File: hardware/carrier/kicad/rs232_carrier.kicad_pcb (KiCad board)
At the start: 2 copper layers, 78 x 95 mm, 133 parts, among them J1 WS header 1-14, J11 RJ45, J12 RJ45, J13 RJ45, J14 RJ45, J2 WS header 15-28, J3 EXT, Q11 2N7002, Q12 AO3401A, Q21 2N7002, Q22 AO3401A, Q31 2N7002, Q32 AO3401A, Q41 2N7002, Q42 AO3401A, U101 TLP2361, U102 TLP2361, U103 MAX3232E, U104 74LVC1G17, U201 TLP2361, U202 TLP2361, U203 MAX3232E, U204 74LVC1G17, U301 TLP2361, U302 TLP2361, U303 MAX3232E, U304 74LVC1G17, U401 TLP2361, U402 TLP2361, U403 MAX3232E, U404 74LVC1G17, U5 MT3608

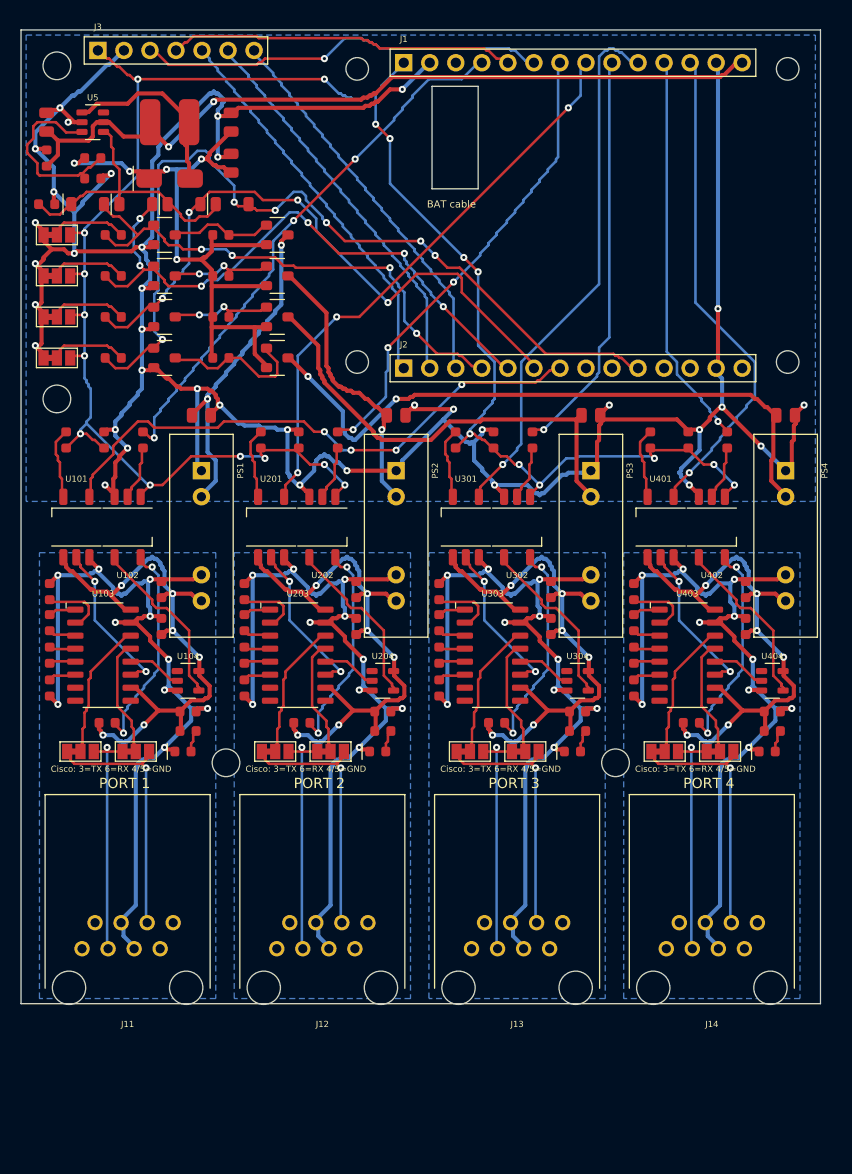
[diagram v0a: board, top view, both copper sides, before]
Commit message: Hardware 0.2: Modul hochkant, Gehäuse zum Zusammenstecken, Akkuklappe
Trägerplatine 78 × 107 mm: Waveshare-Modul hochkant mit USB-C an der
Stirnseite, Versorgung daneben, JST-PH für den Akku auf der Unterseite.
Gehäuse aus drei Teilen ohne Schrauben: Lippe/Nut, vier lösbare Rasthaken,
Pfosten klemmen die Platine, Displayglas als Oberseite, Akkuklappe mit
Rastlasche. Neu geroutet, KiCad-DRC ohne elektrische Fehler.

Co-Authored-By: Claude Fable 5.1 <noreply@anthropic.com>
Claude-Session: https://claude.ai/code/session_01NzB9JfE6QfygfS2yw734Lm
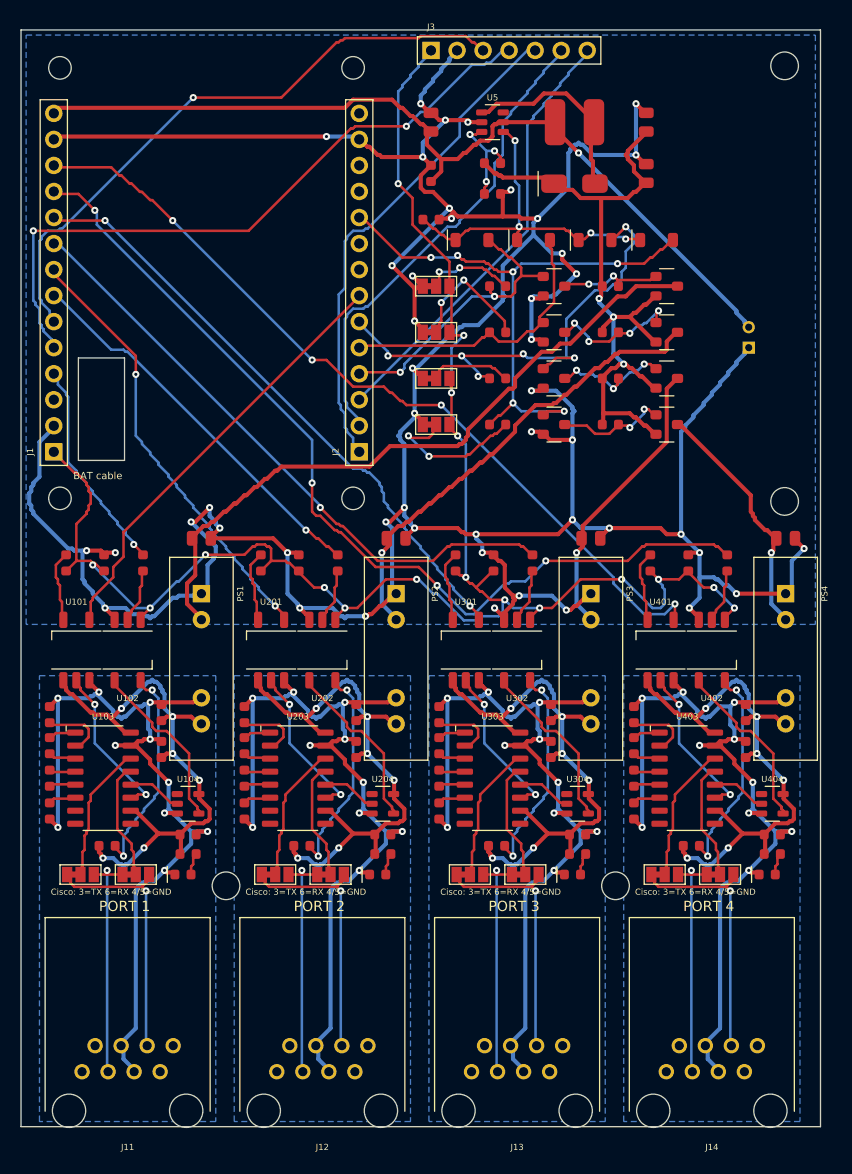
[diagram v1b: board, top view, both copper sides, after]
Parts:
- added J4: BAT JST-PH, rs232fp:JST_PH_2_Vertical, B.Cu at (71.0, 31.0)
- moved H6 71.7 mm to (74.5, 46.0)
- moved H4 71.0 mm to (3.80, 3.70)
- moved H5 71.0 mm to (74.5, 3.50)
- moved H3 51.2 mm to (32.4, 3.70)
- moved J1 51.1 mm to (3.20, 41.2), turned to 90 degrees
- moved H2 51.0 mm to (3.80, 45.7)
- moved D54 41.5 mm to (62.0, 20.5)
- moved C53 40.5 mm to (61.0, 14.0)
- moved C52 40.5 mm to (61.0, 9.00)
- moved D53 40.3 mm to (56.0, 20.5)
- moved D5 39.5 mm to (54.0, 15.0)
- moved L1 39.5 mm to (54.0, 9.00)
- moved R52 39.0 mm to (46.0, 16.0)
- moved R51 39.0 mm to (46.0, 13.0)
- moved U5 39.0 mm to (46.0, 9.00)
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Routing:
- net GND: track 312.0 -> 387.7 mm, vias 36 -> 47
- net ESP_RX4: track 38.5 -> 90.7 mm, vias 1 -> 4
- net ISO_IN4: track 63.8 -> 24.5 mm, vias 2 -> 1
- net ISO_IN1: track 31.9 -> 68.2 mm, vias 2 -> 0
- net ESP_TX4: track 48.3 -> 81.0 mm, vias 1 -> 4
- net ESP_RX1: track 53.3 -> 21.2 mm, vias 3 -> 1
- net SCL: track 34.0 -> 65.9 mm, vias 0 -> 2
- net EN2: track 59.1 -> 29.3 mm, vias 6 -> 0
- net EN4: track 85.2 -> 57.6 mm
- net EN1: track 50.8 -> 29.0 mm, vias 4 -> 2
- net ESP_RX3: track 39.7 -> 60.7 mm
- net SDA: track 40.0 -> 60.7 mm
- net ISO_IN2: track 27.9 -> 47.2 mm
- net +3V3: track 194.9 -> 178.7 mm, vias 22 -> 17
- net ISO_IN3: track 44.5 -> 29.0 mm, vias 0 -> 1
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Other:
- board size 78 x 95 mm -> 78 x 107 mm
- board text added: "Waveshare ESP32-S3-Touch-LCD-2, USB-C up"
- board text removed: "Waveshare ESP32-S3-Touch-LCD-2 (component side down), USB-C ->"

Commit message: Hardware 0.3: Modul mittig, Gehäuse aus Körper und innenliegendem Boden
Trägerplatine: Waveshare-Modul mittig, Versorgung links/rechts aufgeteilt,
RJ45 ganz in der Wand, neu geroutet, DRC ohne elektrische Fehler.
Gehäuse nach Rams/Ive: ein Körper mit durchlaufenden Radien, Glas als
Oberseite, Ziffern vertieft, Boden innenliegend mit sechs Rasthaken,
Akku und J4 nach Abnehmen des Bodens zugänglich; SMA an der Seitenwand.

Co-Authored-By: Claude Fable 5.1 <noreply@anthropic.com>
Claude-Session: https://claude.ai/code/session_01NzB9JfE6QfygfS2yw734Lm
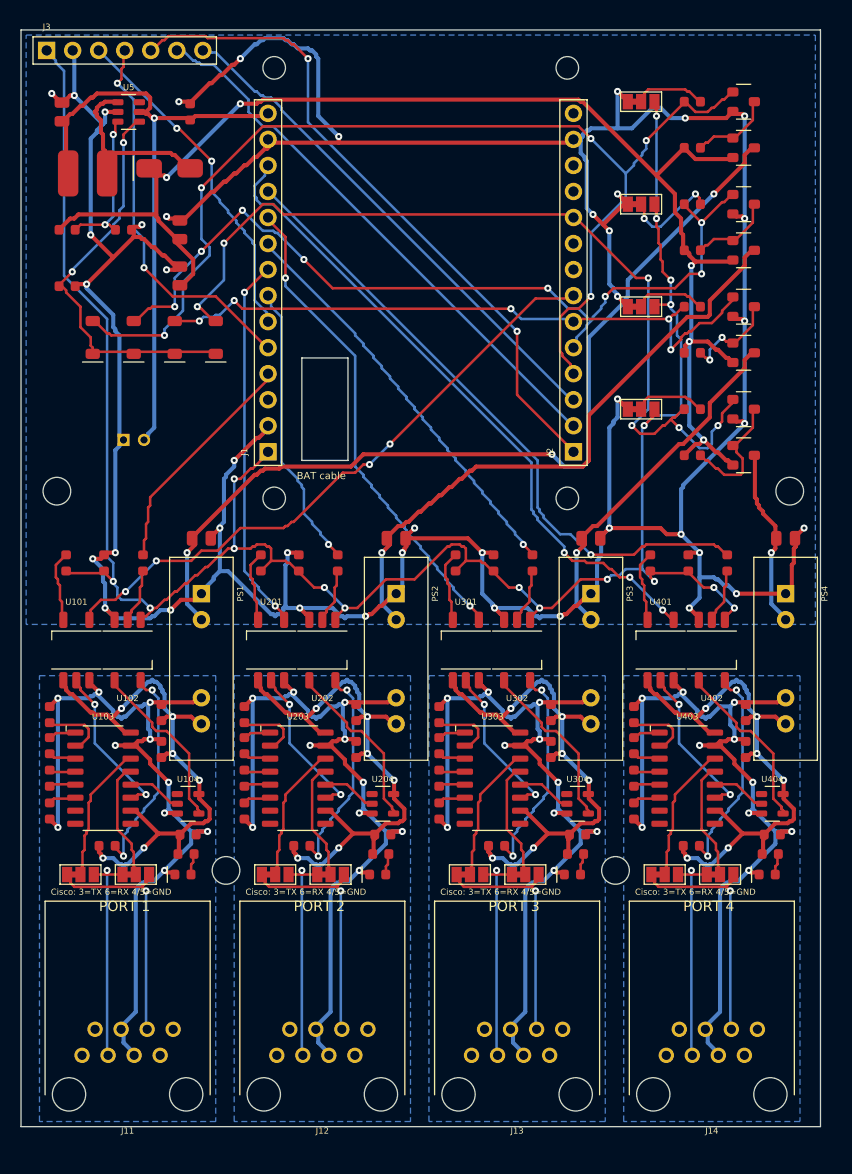
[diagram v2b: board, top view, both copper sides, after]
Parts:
- moved H5 82.2 mm to (3.50, 45.0)
- moved J4 61.7 mm to (10.0, 40.0), turned to 0 degrees
- moved L1 47.8 mm to (6.50, 14.0)
- moved C52 46.7 mm to (15.5, 19.5)
- moved C53 46.6 mm to (15.5, 24.0)
- moved D54 44.0 mm to (19.0, 30.0), turned to 90 degrees
- moved D53 42.1 mm to (15.0, 30.0), turned to 90 degrees
- moved R51 42.0 mm to (4.50, 19.5)
- moved D52 40.1 mm to (11.0, 30.0), turned to 90 degrees
- moved D5 39.5 mm to (14.5, 13.5)
- moved D51 38.2 mm to (7.00, 30.0), turned to 90 degrees
- moved J3 37.5 mm to (2.50, 2.00)
- moved R52 36.2 mm to (10.0, 19.5)
- moved R53 36.1 mm to (4.50, 25.0)
- moved C51 36.0 mm to (4.00, 8.00)
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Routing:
- net EN1: track 29.0 -> 108.7 mm, vias 2 -> 5
- net +5V: track 70.8 -> 135.6 mm, vias 3 -> 5
- net EN2: track 29.3 -> 83.3 mm, vias 0 -> 8
- net +3V3: track 178.7 -> 215.9 mm
- net EN4: track 57.6 -> 87.5 mm
- net SCL: track 65.9 -> 37.8 mm
- net ESP_RX4: track 90.7 -> 63.2 mm, vias 4 -> 1
- net SDA: track 60.7 -> 33.4 mm, vias 1 -> 2
- net VBAT: track 87.9 -> 62.7 mm
- net ISO_IN1: track 68.2 -> 89.9 mm, vias 0 -> 3
- net ESP_RX3: track 60.7 -> 41.0 mm
- net ESP_TX1: track 42.5 -> 60.7 mm, vias 0 -> 4
- net IO2: track 49.1 -> 65.9 mm, vias 0 -> 2
- net ESP_TX4: track 81.0 -> 64.9 mm, vias 4 -> 3
- net EN3: track 49.0 -> 63.6 mm, vias 6 -> 5
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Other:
- outline, holes or cut-outs redrawn

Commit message: Hardware 0.3.1: Maße aus der Waveshare-Zeichnung übernommen
Platine 35,00 × 48,20 mm, Bohrungen 29,00 × 42,20 mm, Glas 37,10 × 58,80 mm
R2,60, Stapel 7,20/9,70 mm, Stiftleisten 30,48 mm. Schaltspalte 1,5 mm nach
rechts, C10 und 2N7002 gedreht (Massepads an der Fläche), Router: Masse-
bäume ohne destruktives Auftrennen (Rip-up mit Rückrollen), Fensterecken
mit Glasradius, Vorschau- und PNG-Rendering in den Skripten, README-Prüfliste
auf die Zeichnung umgestellt.

Co-Authored-By: Claude Fable 5.1 <noreply@anthropic.com>
Claude-Session: https://claude.ai/code/session_01NzB9JfE6QfygfS2yw734Lm
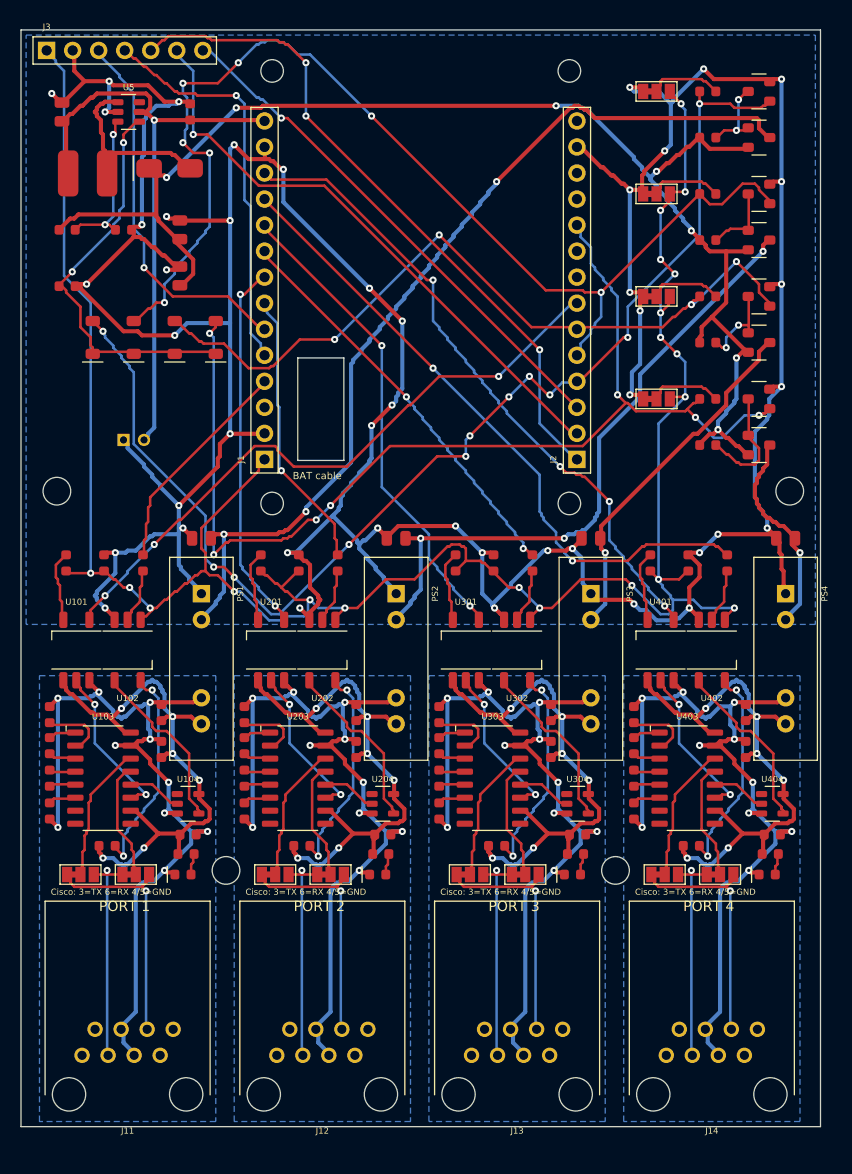
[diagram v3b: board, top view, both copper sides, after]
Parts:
- moved JP11 1.80 mm to (62.0, 6.00)
- moved JP12 1.80 mm to (62.0, 16.0)
- moved JP13 1.80 mm to (62.0, 26.0)
- moved JP14 1.80 mm to (62.0, 36.0)
- moved Q11 1.80 mm to (72.0, 6.00), turned to 180 degrees
- moved Q12 1.80 mm to (72.0, 10.5)
- moved Q21 1.80 mm to (72.0, 16.0), turned to 180 degrees
- moved Q22 1.80 mm to (72.0, 20.5)
- moved Q31 1.80 mm to (72.0, 26.0), turned to 180 degrees
- moved Q32 1.80 mm to (72.0, 30.5)
- moved Q41 1.80 mm to (72.0, 36.0), turned to 180 degrees
- moved Q42 1.80 mm to (72.0, 40.5)
- moved R61 1.80 mm to (67.0, 6.00)
- moved R62 1.80 mm to (67.0, 16.0)
- moved R63 1.80 mm to (67.0, 26.0)
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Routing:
- net EN2: track 83.3 -> 112.3 mm, vias 8 -> 7
- net EN4: track 87.5 -> 107.4 mm, vias 6 -> 7
- net GND: track 399.1 -> 415.8 mm, vias 42 -> 45
- net +3V3: track 215.9 -> 229.9 mm, vias 17 -> 20
- net EN3: track 63.6 -> 75.5 mm, vias 5 -> 4
- net EN1: track 108.7 -> 118.9 mm, vias 5 -> 11
- net SDA: track 33.4 -> 37.2 mm, vias 2 -> 1
- net IO4: track 54.6 -> 58.3 mm, vias 0 -> 1
- net ISO_IN4: track 18.4 -> 21.6 mm
- net ENP2: track 9.34 -> 7.10 mm, vias 2 -> 0
- net ESP_TX1: track 60.7 -> 62.7 mm, vias 4 -> 3
- net PG3: track 10.3 -> 8.46 mm
- net PG2: track 8.84 -> 7.37 mm
- net ISO_IN2: track 61.1 -> 62.6 mm, vias 1 -> 3
- net +5V: track 135.6 -> 137.0 mm, vias 5 -> 7
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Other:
- outline, holes or cut-outs redrawn
